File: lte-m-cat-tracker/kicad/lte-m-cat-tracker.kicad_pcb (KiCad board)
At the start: 2 copper layers, 30 x 35 mm, 33 parts, among them J1 JST-GH-1.25mm-2P, J2 USB-C-16P, SW1 MSK12C02, U1 SIM7080G-M, U2 ESP32-C3, U3 LIS2DW12TR, U4 TP4056, U5 XC6220B331MR-G

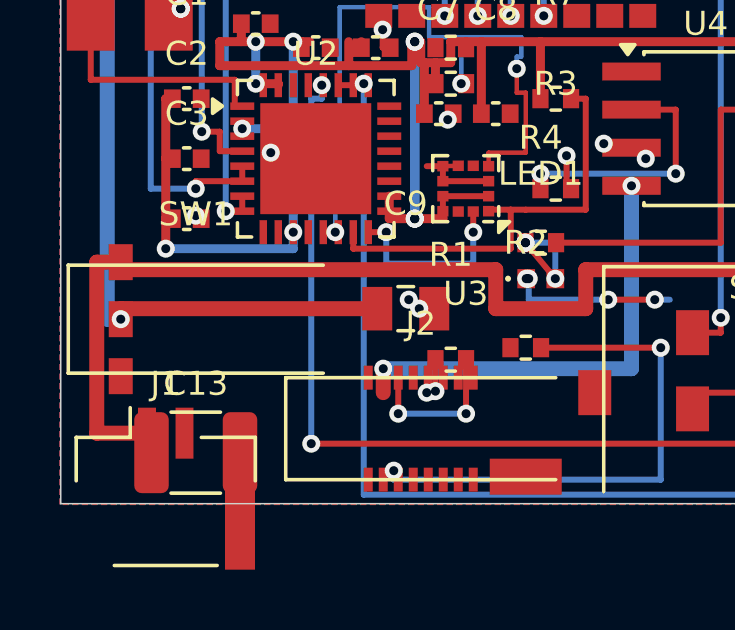
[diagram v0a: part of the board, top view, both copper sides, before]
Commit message: SW1フットプリント修正完了(3件目FPバグ): 実寸パッド+NPTH追加・VBAT/VBAT_SW再配線・DRC通過
- 信号3パッド0.6x1.3ピッチ1.5/NPTH 0.85x2/四隅タブ/本体8x2.8
- DRC: 未接続0/shorts 9(改善)/hole_clearance基線同値/annular 0
Co-Authored-By: Claude Fable 5 <noreply@anthropic.com>
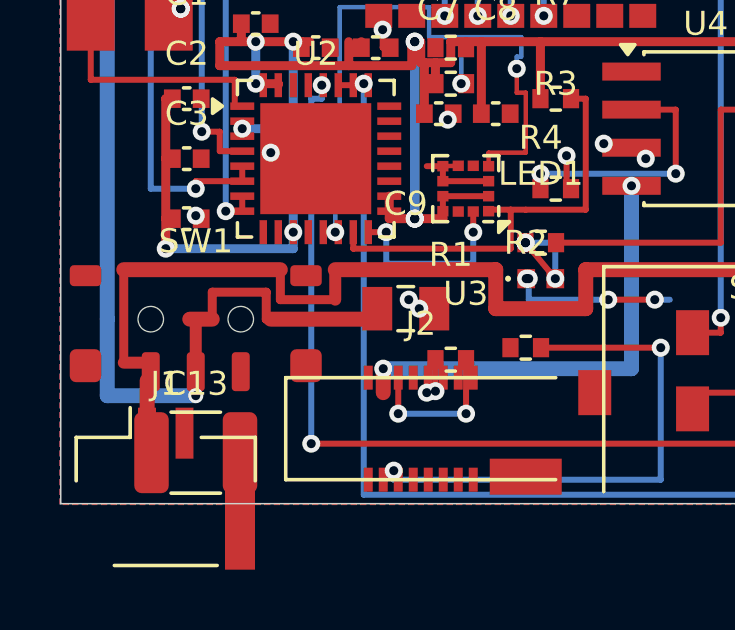
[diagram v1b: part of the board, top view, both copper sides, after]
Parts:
- SW1: value MSK12C02 -> MSK12C02-HB
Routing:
- net VBAT_SW: track 99.6 -> 104.9 mm
- net VBAT: track 36.9 -> 35.9 mm
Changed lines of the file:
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@@
 	(footprint ""
 		(layer "F.Cu")
+		(at 4.5 28.85)
+		(property "Reference" "SW1"
+			(at 0 -2.6 0)
+			(layer "F.SilkS")
+			(effects
+				(font
+					(size 0.8 0.8)
+					(thickness 0.12)
+				)
+			)
+		)
+		(property "Value" "MSK12C02-HB"
+			(at 0 3.2 0)
+			(layer "F.Fab")
+			(effects
+				(font
+					(size 0.8 0.8)
+					(thickness 0.12)
+				)
+			)
+		)
+		(property "Datasheet" ""
+			(at 0 0 0)
+			(layer "F.Fab")
+			(hide yes)
+			(effects
+				(font
+					(size 1.27 1.27)
+				)
+			)
+		)
+		(property "Description" ""
+			(at 0 0 0)
+			(layer "F.Fab")
+			(hide yes)
+			(effects
+				(font
+					(size 1.27 1.27)
+				)
+			)
+		)
+		(duplicate_pad_numbers_are_jumpers no)
+		(fp_rect
+			(start -4.45 -2.05)
+			(end 4.45 2.65)
+			(stroke
+				(width 0.05)
+				(type solid)
+			)
+			(fill no)
+			(layer "F.CrtYd")
+		)
+		(fp_rect
+			(start -4 -1.4)
+			(end 4 1.4)
+			(stroke
+				(width 0.1)
+				(type solid)
+			)
+			(fill no)
+			(layer "F.Fab")
+		)
+		(pad "" np_thru_hole circle
+			(at -1.5 0)
+			(size 0.85 0.85)
+			(drill 0.85)
+			(layers "*.Cu" "*.Mask")
+		)
+		(pad "" np_thru_hole circle
+			(at 1.5 0)
+			(size 0.85 0.85)
+			(drill 0.85)
+			(layers "*.Cu" "*.Mask")
+		)
+		(pad "1" smd roundrect
+			(at -1.5 1.75)
+			(size 0.6 1.3)
+			(layers "F.Cu" "F.Mask" "F.Paste")
+			(roundrect_rratio 0.2)
+			(net "VBAT")
+		)
+		(pad "2" smd roundrect
+			(at 0 1.75)
+			(size 0.6 1.3)
+			(layers "F.Cu" "F.Mask" "F.Paste")
+			(roundrect_rratio 0.2)
+			(net "VBAT_SW")
+		)
+		(pad "3" smd roundrect
+			(at 1.5 1.75)
+			(size 0.6 1.3)
+			(layers "F.Cu" "F.Mask" "F.Paste")
+			(roundrect_rratio 0.2)
+		)
+		(pad "MP1" smd roundrect
+			(at -3.675 -1.45)
+			(size 1.05 0.7)
+			(layers "F.Cu" "F.Mask" "F.Paste")
+			(roundrect_rratio 0.2)
+		)
+		(pad "MP2" smd roundrect
+			(at 3.675 -1.45)
+			(size 1.05 0.7)
+			(layers "F.Cu" "F.Mask" "F.Paste")
+			(roundrect_rratio 0.2)
+		)
+		(pad "MP3" smd roundrect
+			(at -3.675 1.55)
+			(size 1.05 1.1)
+			(layers "F.Cu" "F.Mask" "F.Paste")
+			(roundrect_rratio 0.2)
+		)
+		(pad "MP4" smd roundrect
+			(at 3.675 1.55)
+			(size 1.05 1.1)
+			(layers "F.Cu" "F.Mask" "F.Paste")
+			(roundrect_rratio 0.2)
+		)
+		(embedded_fonts no)
+	)
+	(footprint ""
+		(layer "F.Cu")
 		(at 15 10)
 		(property "Reference" "U1"
@@
 	(footprint ""
 		(layer "F.Cu")
-		(at 4.5 28.85)
-		(property "Reference" "SW1"
-			(at 0 -3.5 0)
-			(layer "F.SilkS")
-			(effects
-				(font
-					(size 0.8 0.8)
-					(thickness 0.12)
-				)
-			)
-		)
-		(property "Value" "MSK12C02"
-			(at 0 3.5 0)
-			(layer "F.Fab")
-			(effects
-				(font
-					(size 0.8 0.8)
-					(thickness 0.12)
-				)
-			)
-		)
-		(property "Datasheet" ""
-			(at 0 0 0)
-			(layer "F.Fab")
-			(hide yes)
-			(effects
-				(font
-					(size 1.27 1.27)
-				)
-			)
-		)
-		(property "Description" ""
-			(at 0 0 0)
-			(layer "F.Fab")
-			(hide yes)
-			(effects
-				(font
-					(size 1.27 1.27)
-				)
-			)
-		)
-		(duplicate_pad_numbers_are_jumpers no)
-		(fp_line
-			(start -4.25 -1.8)
-			(end -4.25 1.8)
-			(stroke
-				(width 0.12)
-				(type default)
-			)
-			(layer "F.SilkS")
-		)
-		(fp_line
-			(start -4.25 -1.8)
-			(end 4.25 -1.8)
-			(stroke
-				(width 0.12)
-				(type default)
-			)
-			(layer "F.SilkS")
-		)
-		(fp_line
-			(start -4.25 1.8)
-			(end 4.25 1.8)
-			(stroke
-				(width 0.12)
-				(type default)
-			)
-			(layer "F.SilkS")
-		)
-		(fp_rect
-			(start -4.5 -2.05)
-			(end 4.5 2.05)
-			(stroke
-				(width 0.05)
-				(type default)
-			)
-			(fill no)
-			(layer "F.CrtYd")
-		)
-		(fp_rect
-			(start -4.25 -1.8)
-			(end 4.25 1.8)
-			(stroke
-				(width 0.1)
-				(type default)
-			)
-			(fill no)
-			(layer "F.Fab")
-		)
-		(pad "1" smd rect
-			(at -2.5 -1.9)
-			(size 0.8 1.2)
-			(layers "F.Cu" "F.Mask" "F.Paste")
-			(net "VBAT")
-			(thermal_bridge_angle 45)
-		)
-		(pad "2" smd rect
-			(at -2.5 0)
-			(size 0.8 1.2)
-			(layers "F.Cu" "F.Mask" "F.Paste")
-			(net "VBAT_SW")
-			(thermal_bridge_angle 45)
-		)
-		(pad "3" smd rect
-			(at -2.5 1.9)
-			(size 0.8 1.2)
-			(layers "F.Cu" "F.Mask" "F.Paste")
-			(thermal_bridge_angle 45)
-		)
-		(embedded_fonts no)
-	)
-	(footprint ""
-		(layer "F.Cu")
 		(at 13 30.2)
 		(property "Reference" "R1"
@@
 	)
 	(segment
-		(start 1.2 32.65)
-		(end 1.2 26.95)
-		(width 0.5)
+		(start 7.32 27.2)
+		(end 7.32 28.2)
+		(width 0.3)
 		(layer "F.Cu")
 		(net "VBAT")
@@
 	)
 	(segment
-		(start 2 27.2)
-		(end 14.5 27.2)
+		(start 2.1 27.2)
+		(end 7.32 27.2)
 		(width 0.5)
 		(layer "F.Cu")
@@
 	)
 	(segment
-		(start 2.875 32.65)
-		(end 1.2 32.65)
+		(start 9.15 27.2)
+		(end 14.5 27.2)
 		(width 0.5)
 		(layer "F.Cu")
@@
 	)
 	(segment
-		(start 1.2 26.95)
-		(end 2 26.95)
+		(start 2.1 30.3)
+		(end 2.1 27.2)
+		(width 0.3)
+		(layer "F.Cu")
+		(net "VBAT")
+	)
+	(segment
+		(start 2.875 32.65)
+		(end 2.88 32.65)
 		(width 0.5)
 		(layer "F.Cu")
@@
 	)
 	(segment
-		(start 2 26.95)
-		(end 2 27.2)
-		(width 0.5)
+		(start 2.7 30.3)
+		(end 2.1 30.3)
+		(width 0.4)
 		(layer "F.Cu")
 		(net "VBAT")
@@
 	)
 	(segment
+		(start 9.15 28.2)
+		(end 9.15 27.2)
+		(width 0.4)
+		(layer "F.Cu")
+		(net "VBAT")
+	)
+	(segment
+		(start 7.32 28.2)
+		(end 9.15 28.2)
+		(width 0.3)
+		(layer "F.Cu")
+		(net "VBAT")
+	)
+	(segment
 		(start 17.5 27.2)
 		(end 24.3 27.2)
@@
 	)
 	(segment
+		(start 2.88 32.65)
+		(end 2.88 30.9)
+		(width 0.5)
+		(layer "F.Cu")
+		(net "VBAT")
+	)
+	(segment
 		(start 22 21.865)
 		(end 22 26.3)
@@
 	)
 	(segment
-		(start 26.3625 22.95)
-		(end 27.4 22.95)
+		(start 4.5 29.95)
+		(end 4.5 28.85)
+		(width 0.4)
+		(layer "F.Cu")
+		(net "VBAT_SW")
+	)
+	(segment
+		(start 5.05 27.95)
+		(end 6.85 27.95)
 		(width 0.3)
 		(layer "F.Cu")
@@
 	)
 	(segment
-		(start 2 28.5)
-		(end 10.55 28.5)
-		(width 0.5)
+		(start 5.05 28.85)
+		(end 5.05 27.95)
+		(width 0.3)
+		(layer "F.Cu")
+		(net "VBAT_SW")
+	)
+	(segment
+		(start 26.3625 22.95)
+		(end 27.4 22.95)
+		(width 0.3)
 		(layer "F.Cu")
 		(net "VBAT_SW")
@@
 	)
 	(segment
-		(start 2 28.85)
-		(end 2 28.5)
-		(width 0.5)
+		(start 6.85 27.95)
+		(end 6.85 28.85)
+		(width 0.3)
 		(layer "F.Cu")
 		(net "VBAT_SW")
@@
 	)
 	(segment
+		(start 7 28.85)
+		(end 10.55 28.85)
+		(width 0.5)
+		(layer "F.Cu")
+		(net "VBAT_SW")
+	)
+	(segment
+		(start 6.85 28.85)
+		(end 7 28.85)
+		(width 0.3)
+		(layer "F.Cu")
+		(net "VBAT_SW")
+	)
+	(segment
 		(start 8.4 6.7)
 		(end 8.4 2.6)
@@
 	)
 	(segment
+		(start 4.3 28.85)
+		(end 5.05 28.85)
+		(width 0.5)
+		(layer "F.Cu")
+		(net "VBAT_SW")
+	)
+	(segment
 		(start 10.6 6.7)
 		(end 8.4 6.7)
@@
 	)
 	(via
-		(at 2 28.85)
-		(size 0.6)
+		(at 4.5 31.4)
+		(size 0.5)
 		(drill 0.3)
 		(layers "F.Cu" "B.Cu")
@@
 	)
 	(segment
-		(start 1.55 28.85)
-		(end 2 28.85)
+		(start 4.5 31.4)
+		(end 1.55 31.4)
+		(width 0.5)
+		(layer "B.Cu")
+		(net "VBAT_SW")
+	)
+	(segment
+		(start 1.55 31.4)
+		(end 1.55 28.85)
 		(width 0.5)
 		(layer "B.Cu")

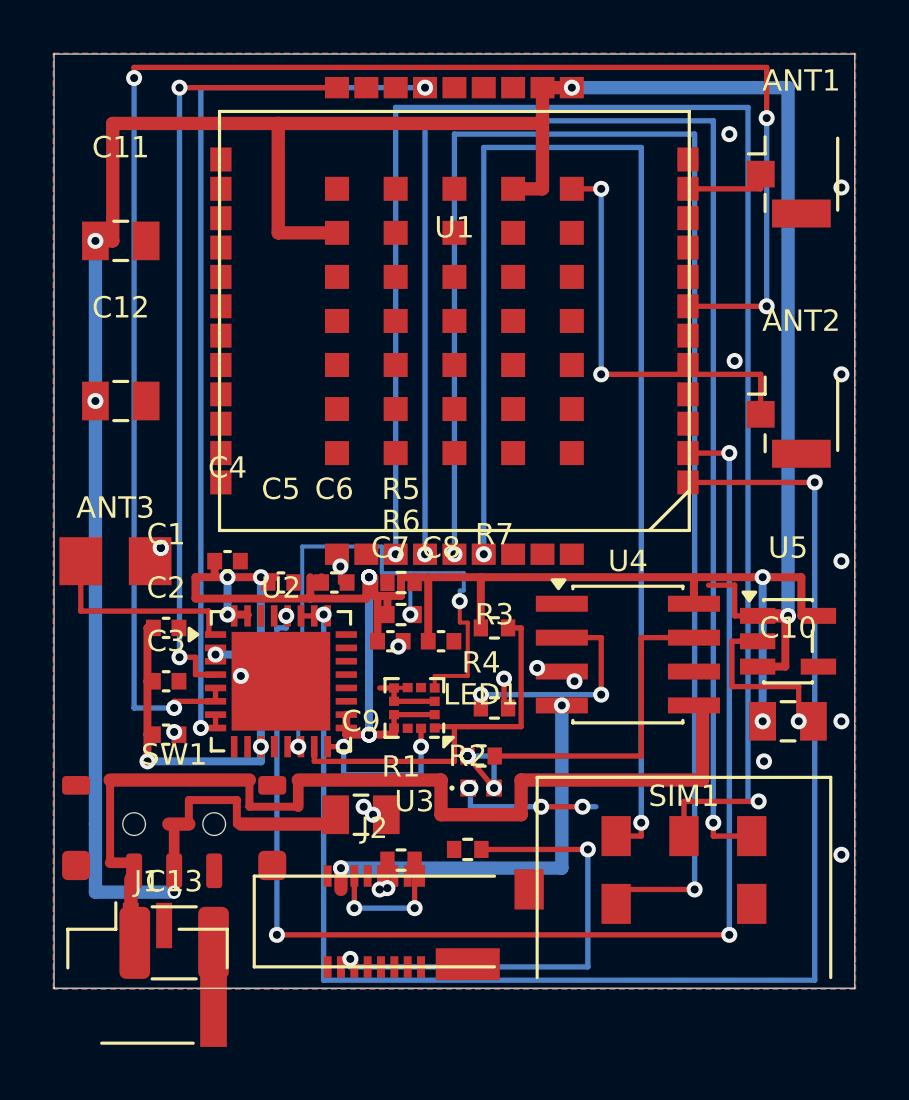
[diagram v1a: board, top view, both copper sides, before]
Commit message: 致命修正#2完了: 40MHz水晶Y1(HD 7D040000M01/2016)+C16/C17をPCB実装・DRC通過・BOM/CPL更新
- XTAL_N/P全F.Cu via0本(y19.72/y20.0バンド→x16.0/x16.7降下)
- 部品5点移設(C5/C6/C8/R5/R7)・+3.3V再配管(ダイブ/via-A/Bリンク/スパイン)
- DRC: shorts実質基準値・crossings0・未接続はゾーン浮き断片1のみ
- 残: 回路図へのY1/C16/C17反映
Co-Authored-By: Claude Fable 5 <noreply@anthropic.com>
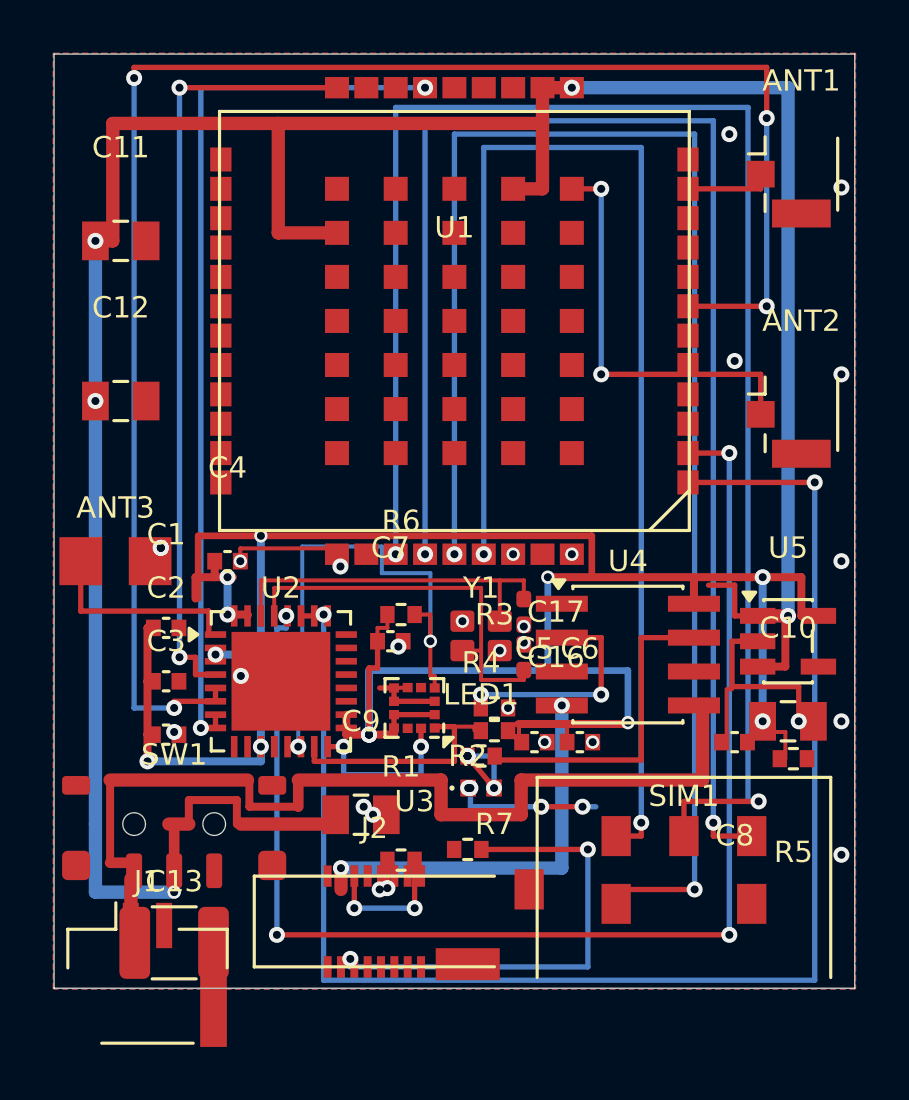
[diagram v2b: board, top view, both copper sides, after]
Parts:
- added C16: 18pF, , F.Cu at (17.6, 22.6)
- added C17: 18pF, , F.Cu at (17.6, 20.9)
- added Y1: 7D040000M01 40MHz 12pF, , F.Cu at (16.0, 21.8)
- moved R5 16.1 mm to (27.7, 26.4), turned to 180 degrees
- moved C8 11.6 mm to (25.5, 25.8), turned to 180 degrees
- moved C5 11.2 mm to (18.0, 25.8)
- moved C6 11.0 mm to (19.7, 25.8)
- moved R7 3.85 mm to (16.5, 25.4), turned to 180 degrees
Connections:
- U2 pad 29: (no net) -> XTAL_N
- U2 pad 30: (no net) -> XTAL_P
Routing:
- net XTAL_N: track 0.00 -> 14.0 mm
- net XTAL_P: track 0.00 -> 12.3 mm
- net +3.3V: track 83.5 -> 95.0 mm
- net I2C_SCL: track 14.6 -> 8.79 mm
- net GND: track 19.1 -> 22.8 mm, vias 26 -> 32
- net I2C_SDA: track 22.4 -> 19.0 mm, vias 3 -> 2

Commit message: 🔴 致命的バグ修正: UARTをUART2(pad22/23)からAT用UART1(pad1/2)へ付替
- EasyEDA C18548266正式ピン表+HW Design V1.03で全77パッド照合
- UART2はDAM専用でAT不可→発注していればAT通信不能だった
- VDD_EXT(pad40)新設・NC誤接続撤去(46/47,28)・旧配線55セグメント削除
- DRC: 違反248→229・短絡10→5・未配線6は付替ネットの再配線待ち

Co-Authored-By: Claude Fable 5 <noreply@anthropic.com>
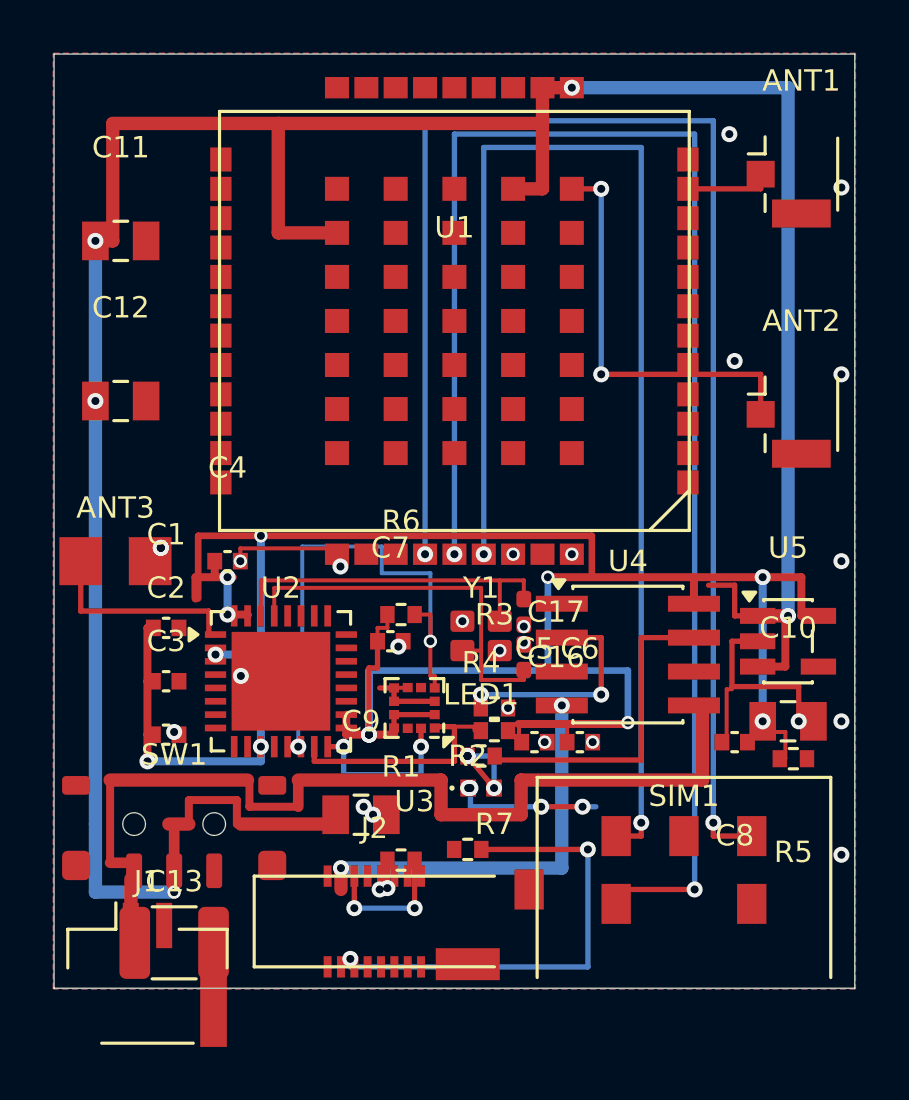
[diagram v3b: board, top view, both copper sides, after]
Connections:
- U1 pad 1: (no net) -> SIM_TXD
- U1 pad 2: (no net) -> SIM_RXD
- U1 pad 22: SIM_TXD -> (no net)
- U1 pad 23: SIM_RXD -> (no net)
- U1 pad 28: SIM_RESETN -> (no net)
- U1 pad 40: (no net) -> VDD_EXT
- U1 pad 46: VBAT_SW -> (no net)
- U1 pad 47: VBAT_SW -> (no net)
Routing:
- net SIM_RESETN: track 63.4 -> 0.00 mm, vias 4 -> 0
- net SIM_DATA: track 60.4 -> 0.00 mm, vias 2 -> 0
- net SIM_TXD: track 56.4 -> 0.00 mm, vias 2 -> 0
- net SIM_RXD: track 48.9 -> 0.00 mm, vias 4 -> 0
- net SIM_PWRKEY: track 33.4 -> 0.00 mm, vias 2 -> 0
- net SIM_STATUS: track 29.2 -> 0.00 mm, vias 2 -> 0

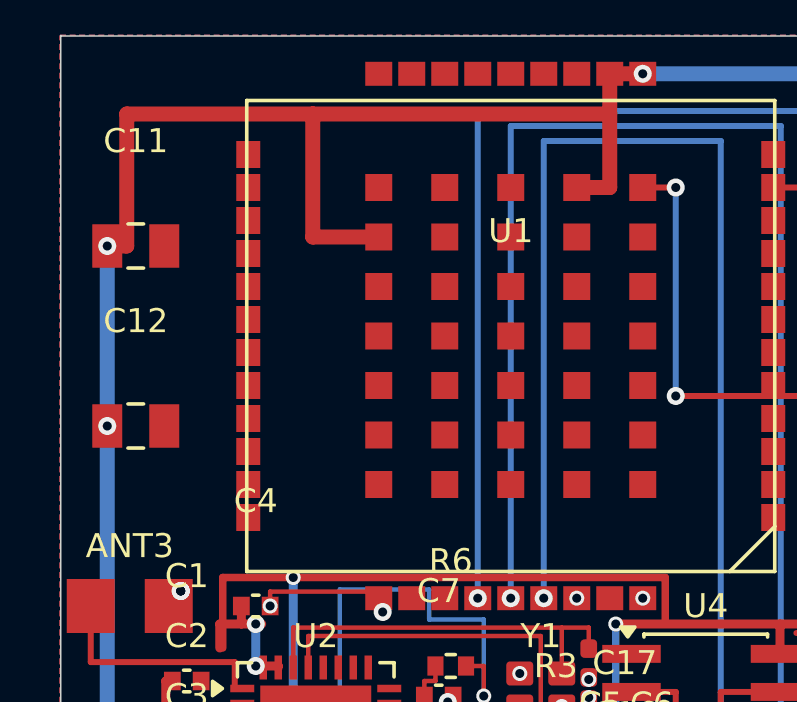
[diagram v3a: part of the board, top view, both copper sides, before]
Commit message: レベルシフタU6(TXB0104RGYR/VQFN-14)実装完了: 配置・ネット分割・VBAT_SW幹線B.Cu移設
- TSSOP-14は盤面に入らずRGY(3.5x3.5mm)へ変更(C400708)
- TIランドパターン+EasyEDA照合・EP1.7mm縮小(JLCPCB製造性)
- C12移動・C18/C19パスコン追加・U2を_33ネットへ付替
- DRC: 違反243・短絡3(J2既存のみ)・未配線14(配線再実行待ち)

Co-Authored-By: Claude Fable 5 <noreply@anthropic.com>
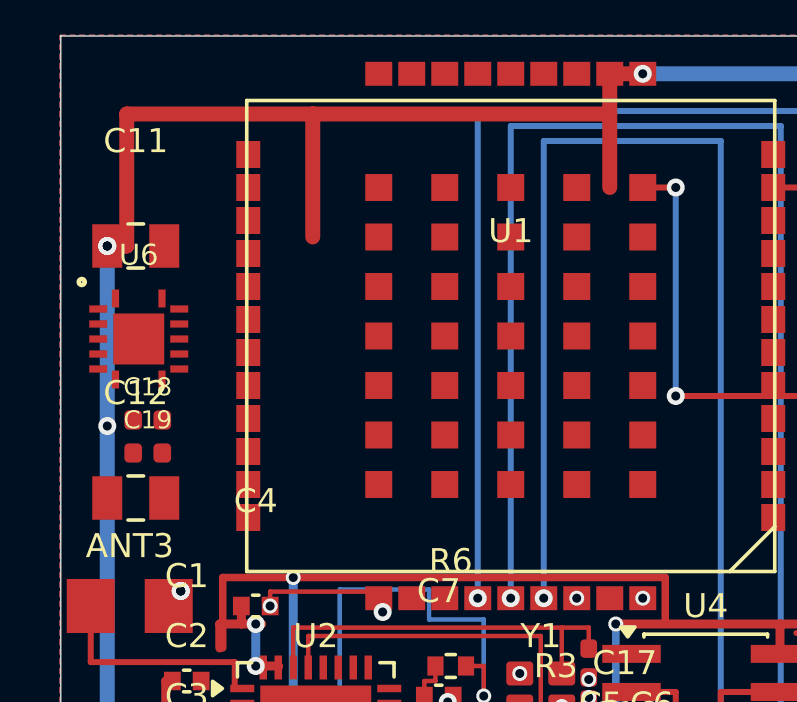
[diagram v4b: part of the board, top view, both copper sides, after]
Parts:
- added C18: 100nF, lte-m-custom:C_0402, F.Cu at (2.90, 12.8)
- added C19: 100nF, lte-m-custom:C_0402, F.Cu at (2.90, 13.9)
- added U6: TXB0104RGYR, lte-m-custom:TXB0104_RGY14, F.Cu at (2.60, 10.1)
- moved C12 2.40 mm to (2.50, 15.4)
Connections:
- U2 pad 27: SIM_TXD -> SIM_TXD_33
- U2 pad 28: SIM_RXD -> SIM_RXD_33
- U2 pad 4: SIM_STATUS -> SIM_STATUS_33
- U2 pad 6: SIM_RESETN -> (no net)
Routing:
- net VBAT_SW: track 104.9 -> 101.6 mm, vias 5 -> 6
